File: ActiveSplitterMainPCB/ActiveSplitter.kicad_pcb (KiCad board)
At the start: 2 copper layers, 78 x 31 mm, 24 parts, among them J1 SMA_EDGE, J2 SMA_EDGE, J3 SMA_EDGE, J4 SMA_EDGE, J5 SMA_EDGE, J6 Conn_01x28_Pin, J7 Conn_01x28_Pin, J8 Conn_01x12_Pin, J9 Conn_01x12_Pin, U1 PSA4-5043

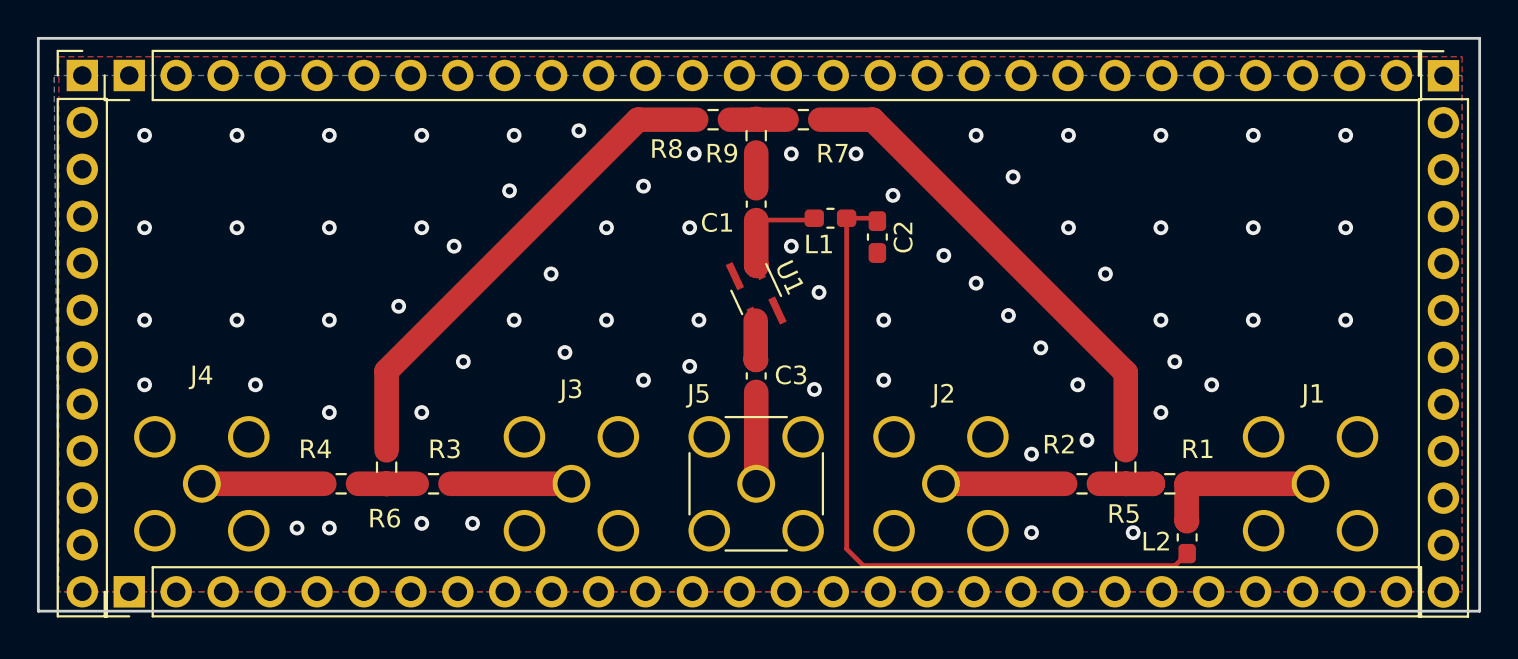
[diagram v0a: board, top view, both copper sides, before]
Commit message: add termination resistors, PDF and SVG outputs for viewing
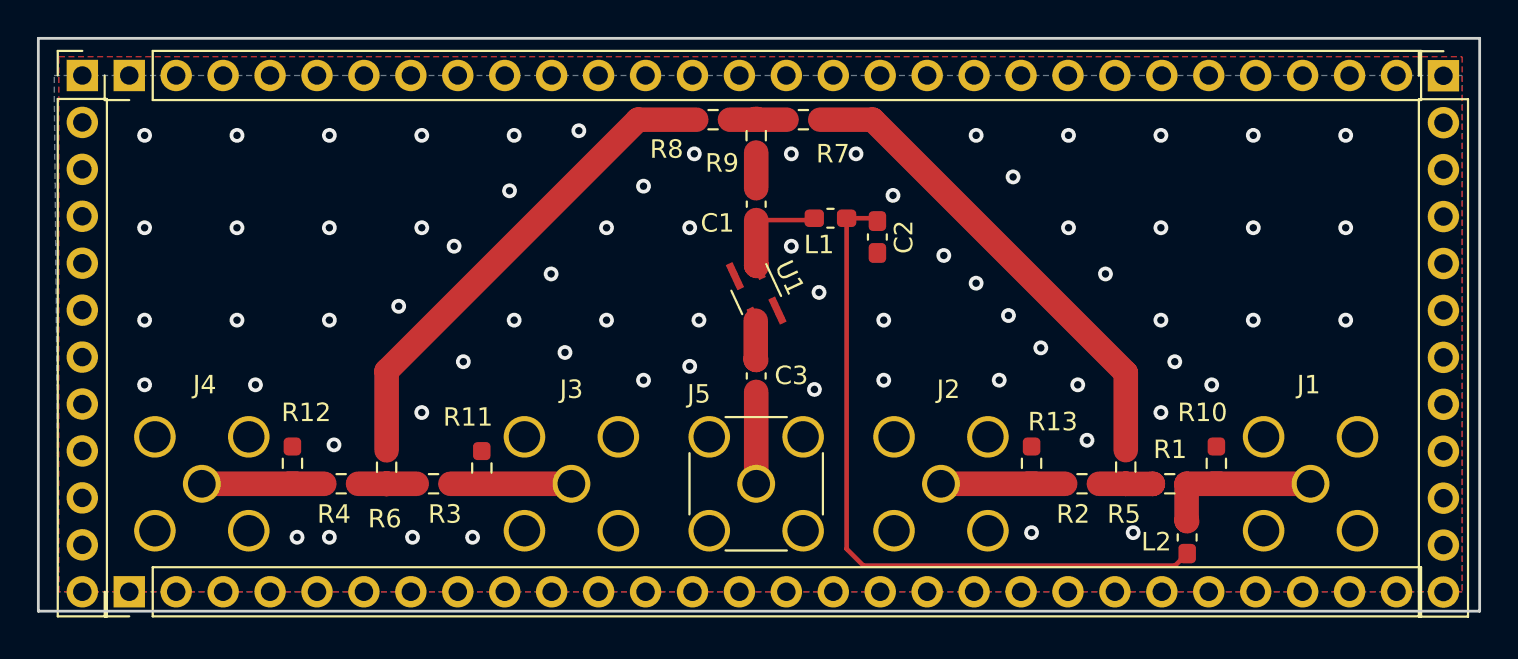
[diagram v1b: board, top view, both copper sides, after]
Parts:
- added R10: DNP, Resistor_SMD:R_0603_1608Metric_Pad0.98x0.95mm_HandSolder, F.Cu at (164.8, 101.0)
- added R11: DNP, Resistor_SMD:R_0603_1608Metric_Pad0.98x0.95mm_HandSolder, F.Cu at (125.0, 101.2)
- added R12: DNP, Resistor_SMD:R_0603_1608Metric_Pad0.98x0.95mm_HandSolder, F.Cu at (114.8, 101.0)
- added R13: DNP, Resistor_SMD:R_0603_1608Metric_Pad0.98x0.95mm_HandSolder, F.Cu at (154.8, 101.0)
- R1, R2, R3, R4, R5, R6, R7, R8, R9: value R -> 30

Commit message: Reduced output SMA spacing to 17mm to match USB hub.  Added pad for external 3V supply.
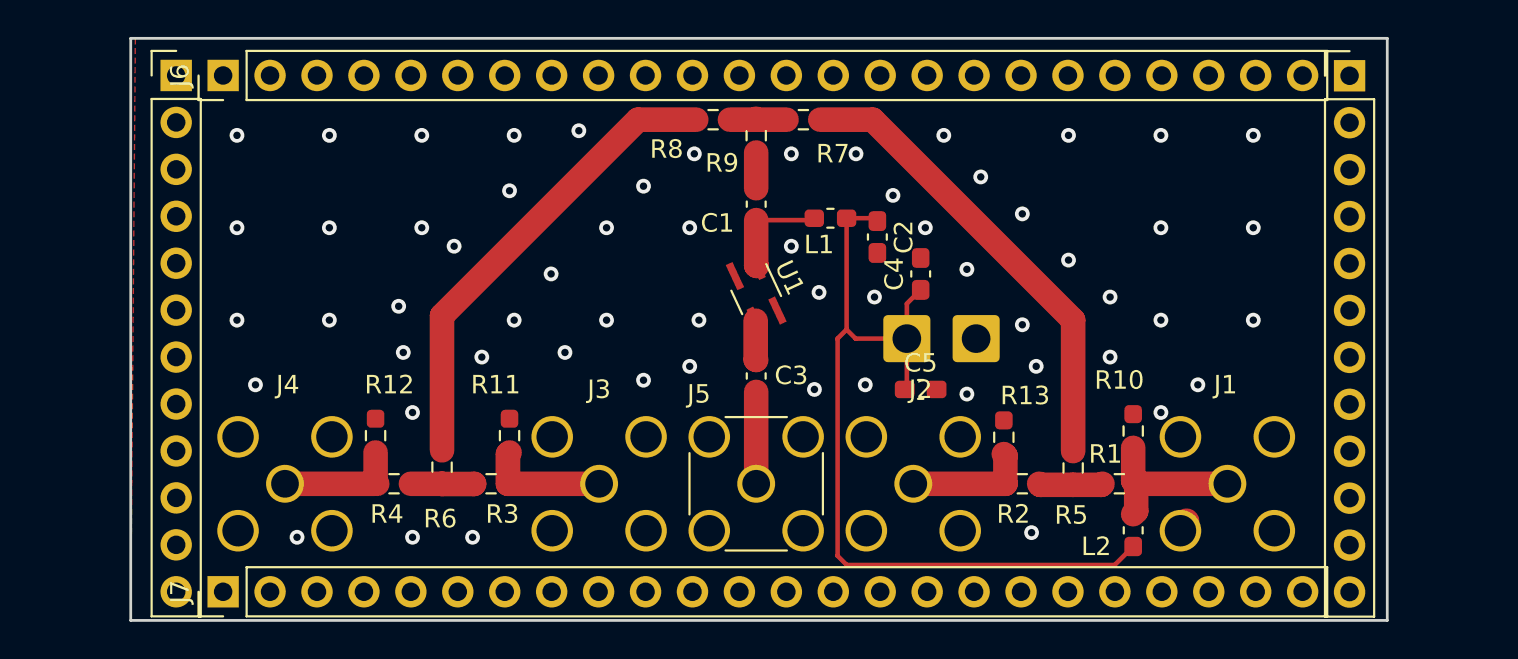
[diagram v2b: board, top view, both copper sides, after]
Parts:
- added C4: 100p, Capacitor_SMD:C_0603_1608Metric_Pad1.08x0.95mm_HandSolder, F.Cu at (148.8, 90.8)
- added C5: 100p, Capacitor_SMD:C_0603_1608Metric_Pad1.08x0.95mm_HandSolder, F.Cu at (148.8, 97.0)
- added J10: Conn_01x01_Pin, Connector_Wire:SolderWire-0.75sqmm_1x01_D1.25mm_OD2.3mm, F.Cu at (148.0, 94.2)
- added J11: Conn_01x01_Pin, Connector_Wire:SolderWire-0.75sqmm_1x01_D1.25mm_OD2.3mm, F.Cu at (151.8, 94.2)
- J6, J7: value Conn_01x28_Pin -> Conn_01x24_Pin; footprint Connector_PinHeader_2.54mm:PinHeader_1x28_P2.54mm_Vertical -> Connector_PinHeader_2.54mm:PinHeader_1x24_P2.54mm_Vertical
- moved J6 5.08 mm to (111.0, 80.0)
- moved J7 5.08 mm to (111.0, 108.0)
- moved J8 5.08 mm to (108.5, 80.0)
- moved J9 5.08 mm to (172.0, 80.0)
- moved R10 4.83 mm to (160.2, 99.2)
- moved R12 4.74 mm to (119.2, 99.5)
- moved J1 4.50 mm to (165.3, 102.1)
- moved J4 4.50 mm to (114.3, 102.1)
- moved R2 3.23 mm to (154.2, 102.1)
- moved R3 3.11 mm to (125.5, 102.1)
- moved R6 3.00 mm to (122.8, 101.2)
- moved L2 2.95 mm to (160.2, 104.6)
- moved R4 2.86 mm to (120.2, 102.1)
- moved R5 2.85 mm to (157.0, 101.2)
- moved R1 2.73 mm to (159.5, 102.1)
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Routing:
- net +3V3: track 38.7 -> 46.0 mm
- net Net-(R6-Pad1): track 26.7 -> 25.4 mm
- net Net-(R5-Pad1): track 26.4 -> 25.3 mm
- net Net-(R1-Pad2): track 2.92 -> 3.47 mm
- net GND: track 0.00 -> 0.04 mm, vias 70 -> 62
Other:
- board size 78 x 31 mm -> 68 x 31.5 mm
